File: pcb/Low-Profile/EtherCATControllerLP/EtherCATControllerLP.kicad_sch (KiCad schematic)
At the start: 0 parts

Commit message: checkpoint
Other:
- added sheet Temperature Sensors (Temperature.kicad_sch)
- sheet MCU ports: added TEMP_BACKSIDE, TEMP_ICS, TEMP_MOSFETS; removed none
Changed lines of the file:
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@@
+		)
+	)
+	(label "TEMP_BACKSIDE"
+		(at 99.06 107.95 0)
+		(fields_autoplaced yes)
+		(effects
+			(font
+				(size 1.27 1.27)
+			)
+			(justify left bottom)
 		)
 	)
@@
 		)
 	)
+	(label "TEMP_ICS"
+		(at 207.01 93.98 180)
+		(fields_autoplaced yes)
+		(effects
+			(font
+				(size 1.27 1.27)
+			)
+			(justify right bottom)
+		)
+	)
 	(label "SPI2_SCK"
 		(at 173.99 35.56 0)
@@
 		)
 	)
+	(label "TEMP_ICS"
+		(at 99.06 105.41 0)
+		(fields_autoplaced yes)
+		(effects
+			(font
+				(size 1.27 1.27)
+			)
+			(justify left bottom)
+		)
+	)
 	(label "ETH0_TXN"
 		(at 146.05 105.41 180)
@@
 		)
 	)
+	(label "TEMP_MOSFETS"
+		(at 99.06 102.87 0)
+		(fields_autoplaced yes)
+		(effects
+			(font
+				(size 1.27 1.27)
+			)
+			(justify left bottom)
+		)
+	)
 	(label "PGOOD"
 		(at 99.06 86.36 0)
@@
 		)
 	)
+	(label "TEMP_MOSFETS"
+		(at 207.01 91.44 180)
+		(fields_autoplaced yes)
+		(effects
+			(font
+				(size 1.27 1.27)
+			)
+			(justify right bottom)
+		)
+	)
 	(label "SPI_MOSI"
 		(at 207.01 48.26 180)
@@
 			)
 			(justify left bottom)
+		)
+	)
+	(label "TEMP_BACKSIDE"
+		(at 207.01 96.52 180)
+		(fields_autoplaced yes)
+		(effects
+			(font
+				(size 1.27 1.27)
+			)
+			(justify right bottom)
 		)
 	)
@@
 	)
 	(sheet
+		(at 71.12 100.33)
+		(size 27.94 10.16)
+		(fields_autoplaced yes)
+		(stroke
+			(width 0.1524)
+			(type solid)
+		)
+		(fill
+			(color 0 0 0 0.0000)
+		)
+		(property "Sheetname" "Temperature Sensors"
+			(at 71.12 99.6184 0)
+			(effects
+				(font
+					(size 1.27 1.27)
+				)
+				(justify left bottom)
+			)
+		)
+		(property "Sheetfile" "Temperature.kicad_sch"
+			(at 71.12 111.0746 0)
+			(effects
+				(font
+					(size 1.27 1.27)
+				)
+				(justify left top)
+			)
+		)
+		(pin "TEMP_MOSFETS" output
+			(at 99.06 102.87 0)
+			(effects
+				(font
+					(size 1.27 1.27)
+				)
+				(justify right)
+			)
+		)
+		(pin "TEMP_ICS" output
+			(at 99.06 105.41 0)
+			(effects
+				(font
+					(size 1.27 1.27)
+				)
+				(justify right)
+			)
+		)
+		(pin "TEMP_BACKSIDE" output
+			(at 99.06 107.95 0)
+			(effects
+				(font
+					(size 1.27 1.27)
+				)
+				(justify right)
+			)
+		)
+		(instances
+			(project "EtherCATControllerLP"
+				(path "/4c927f80-855d-490a-80b2-e5c55283621a"
+					(page "10")
+				)
+			)
+		)
+	)
+	(sheet
 		(at 71.12 24.13)
 		(size 27.94 49.53)
@@
 	(sheet
 		(at 207.01 25.4)
-		(size 29.21 64.77)
+		(size 29.21 73.66)
 		(fields_autoplaced yes)
 		(stroke
@@
 		)
 		(property "Sheetfile" "MCU.kicad_sch"
-			(at 207.01 90.7546 0)
+			(at 207.01 99.6446 0)
 			(effects
 				(font
@@
 			(effects
 				(font
+					(size 1.27 1.27)
+				)
+				(justify left)
+			)
+		)
+		(pin "TEMP_ICS" input
+			(at 207.01 91.44 180)
+			(effects
+				(font
+					(size 1.27 1.27)
+				)
+				(justify left)
+			)
+		)
+		(pin "TEMP_BACKSIDE" input
+			(at 207.01 93.98 180)
+			(effects
+				(font
+					(size 1.27 1.27)
+				)
+				(justify left)
+			)
+		)
+		(pin "TEMP_MOSFETS" input
+			(at 207.01 96.52 180)
+			(effects
+				(font

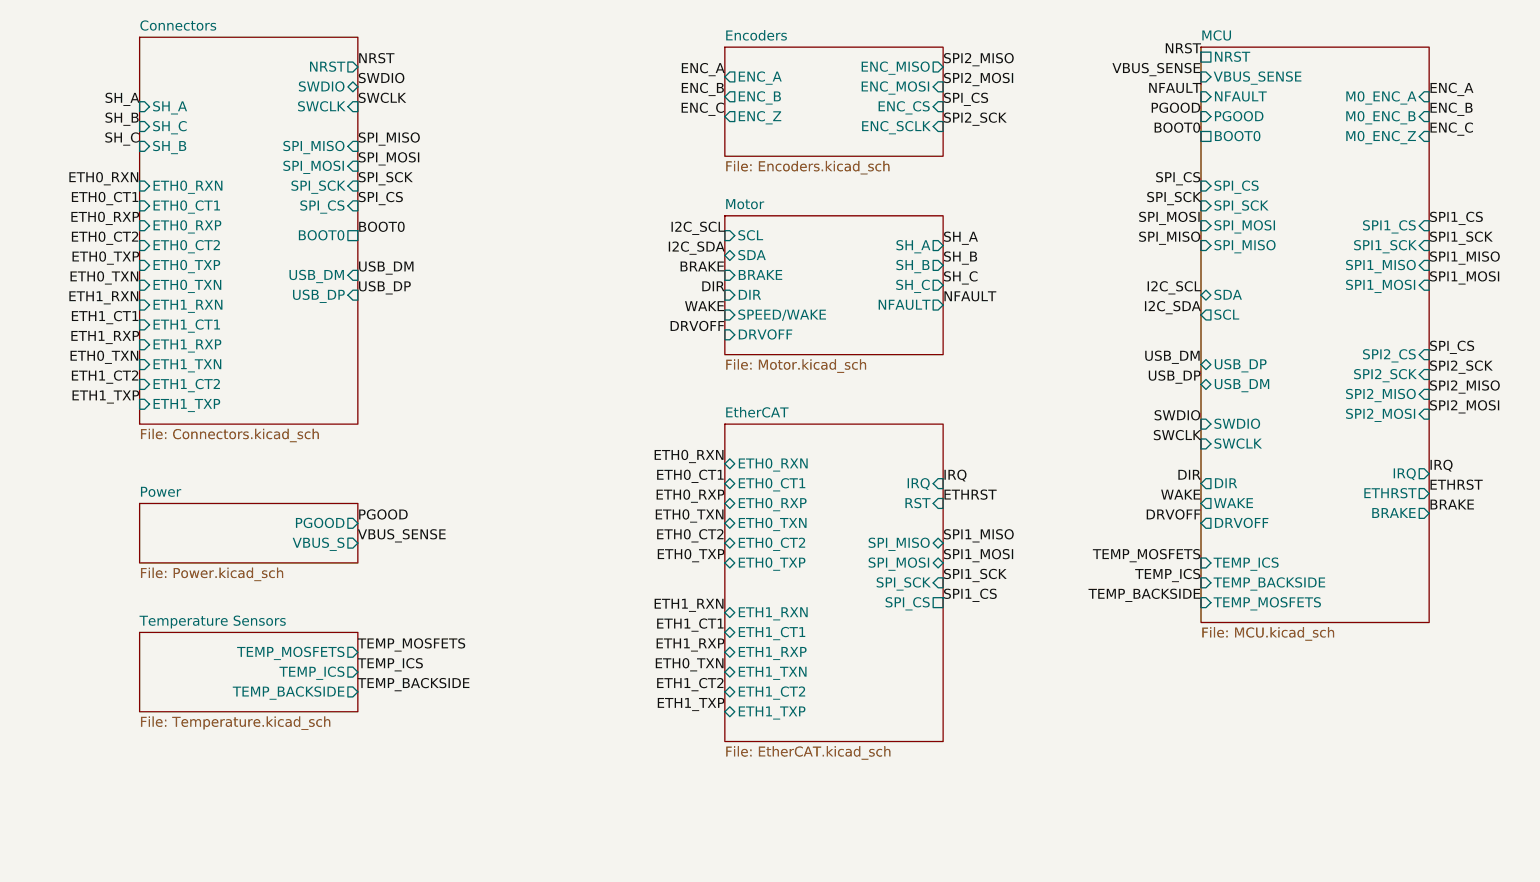
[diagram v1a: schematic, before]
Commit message: Checkpoint changes before switching to XMC4800
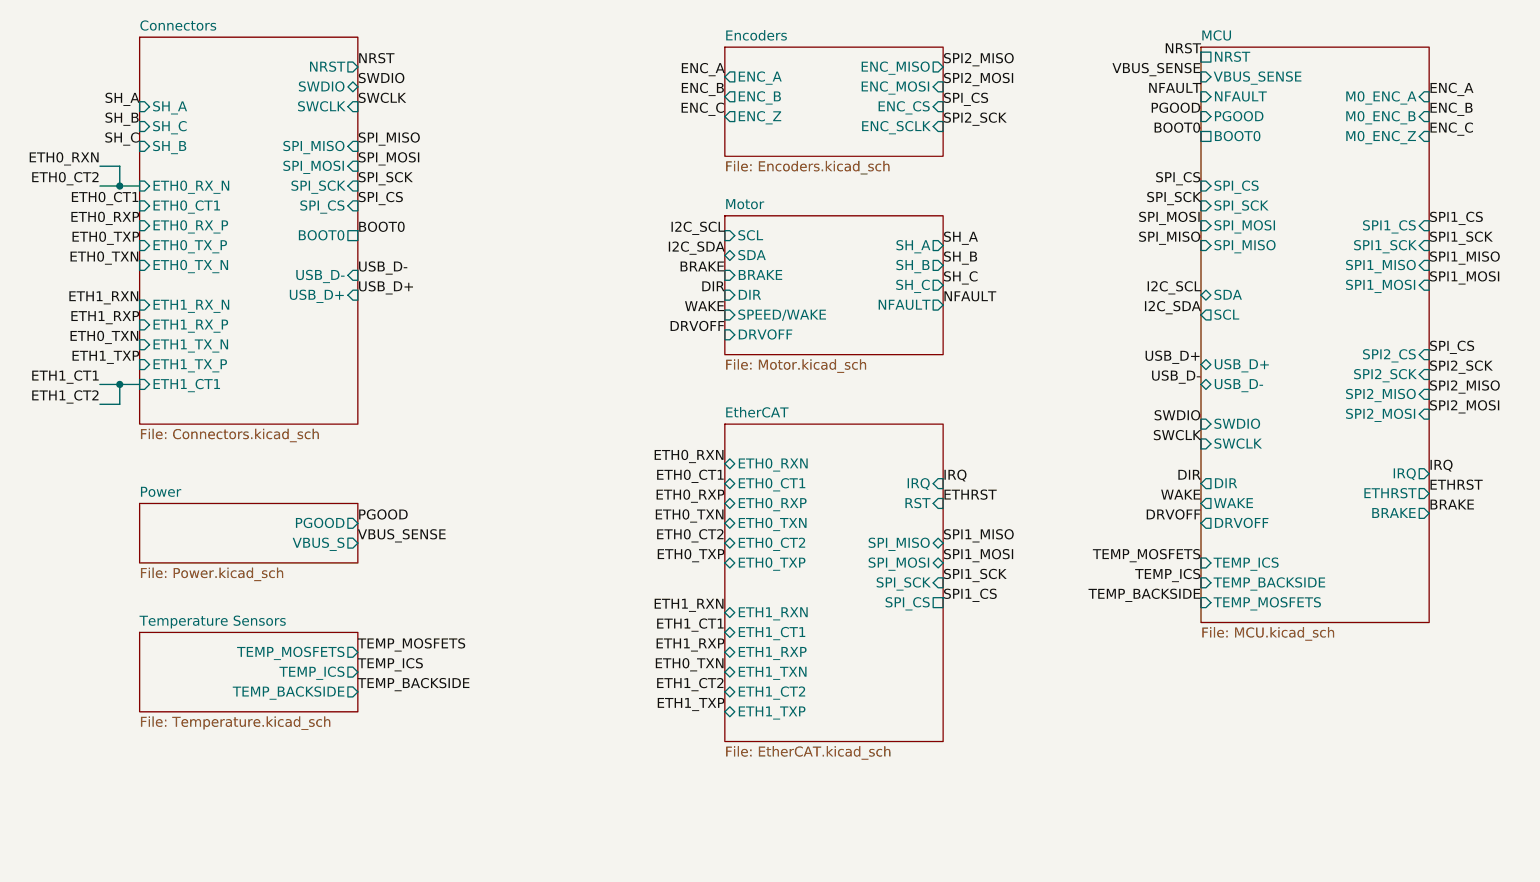
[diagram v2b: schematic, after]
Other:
- sheet Connectors ports: added ETH0_RX_N, ETH0_RX_P, ETH0_TX_N, ETH0_TX_P, ETH1_RX_N, ETH1_RX_P, ETH1_TX_N, ETH1_TX_P, USB_D+, USB_D-; removed ETH0_CT2, ETH0_RXN, ETH0_RXP, ETH0_TXN, ETH0_TXP, ETH1_CT2, ETH1_RXN, ETH1_RXP, ETH1_TXN, ETH1_TXP, USB_DM, USB_DP
- sheet MCU ports: added USB_D+, USB_D-; removed USB_DM, USB_DP

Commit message: Finished new 2+2 IOboard
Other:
- added sheet CAN (CAN.kicad_sch)
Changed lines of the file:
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@@
+	)
+	(sheet
+		(at 71.12 117.475)
+		(size 27.94 10.16)
+		(fields_autoplaced yes)
+		(stroke
+			(width 0.1524)
+			(type solid)
+		)
+		(fill
+			(color 0 0 0 0.0000)
+		)
+		(property "Sheetname" "CAN"
+			(at 71.12 116.7634 0)
+			(effects
+				(font
+					(size 1.27 1.27)
+				)
+				(justify left bottom)
+			)
+		)
+		(property "Sheetfile" "CAN.kicad_sch"
+			(at 71.12 128.2196 0)
+			(effects
+				(font
+					(size 1.27 1.27)
+				)
+				(justify left top)
+			)
+		)
+		(pin "CAN_TX" bidirectional
+			(at 71.12 120.015 180)
+			(effects
+				(font
+					(size 1.27 1.27)
+				)
+				(justify left)
+			)
+		)
+		(pin "CAN_RX" bidirectional
+			(at 71.12 122.555 180)
+			(effects
+				(font
+					(size 1.27 1.27)
+				)
+				(justify left)
+			)
+		)
+		(pin "CAN_MODE" output
+			(at 71.12 125.095 180)
+			(effects
+				(font
+					(size 1.27 1.27)
+				)
+				(justify left)
+			)
+		)
+		(pin "CAN_H" input
+			(at 99.06 120.015 0)
+			(effects
+				(font
+					(size 1.27 1.27)
+				)
+				(justify right)
+			)
+		)
+		(pin "CAN_L" input
+			(at 99.06 123.825 0)
+			(effects
+				(font
+					(size 1.27 1.27)
+				)
+				(justify right)
+			)
+		)
+		(instances
+			(project "EtherCATControllerLP"
+				(path "/4c927f80-855d-490a-80b2-e5c55283621a"
+					(page "11")
+				)
+			)
+		)
 	)
 	(sheet
